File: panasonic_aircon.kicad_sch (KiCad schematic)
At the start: 24 parts, among them J1 Conn_01x04, Q1 BSS138, Q2 BSS138, SW1 SW_Push, U1 ESP32-WROOM-32, U2 AP2112K-3.3, U3 ESP_Programmer

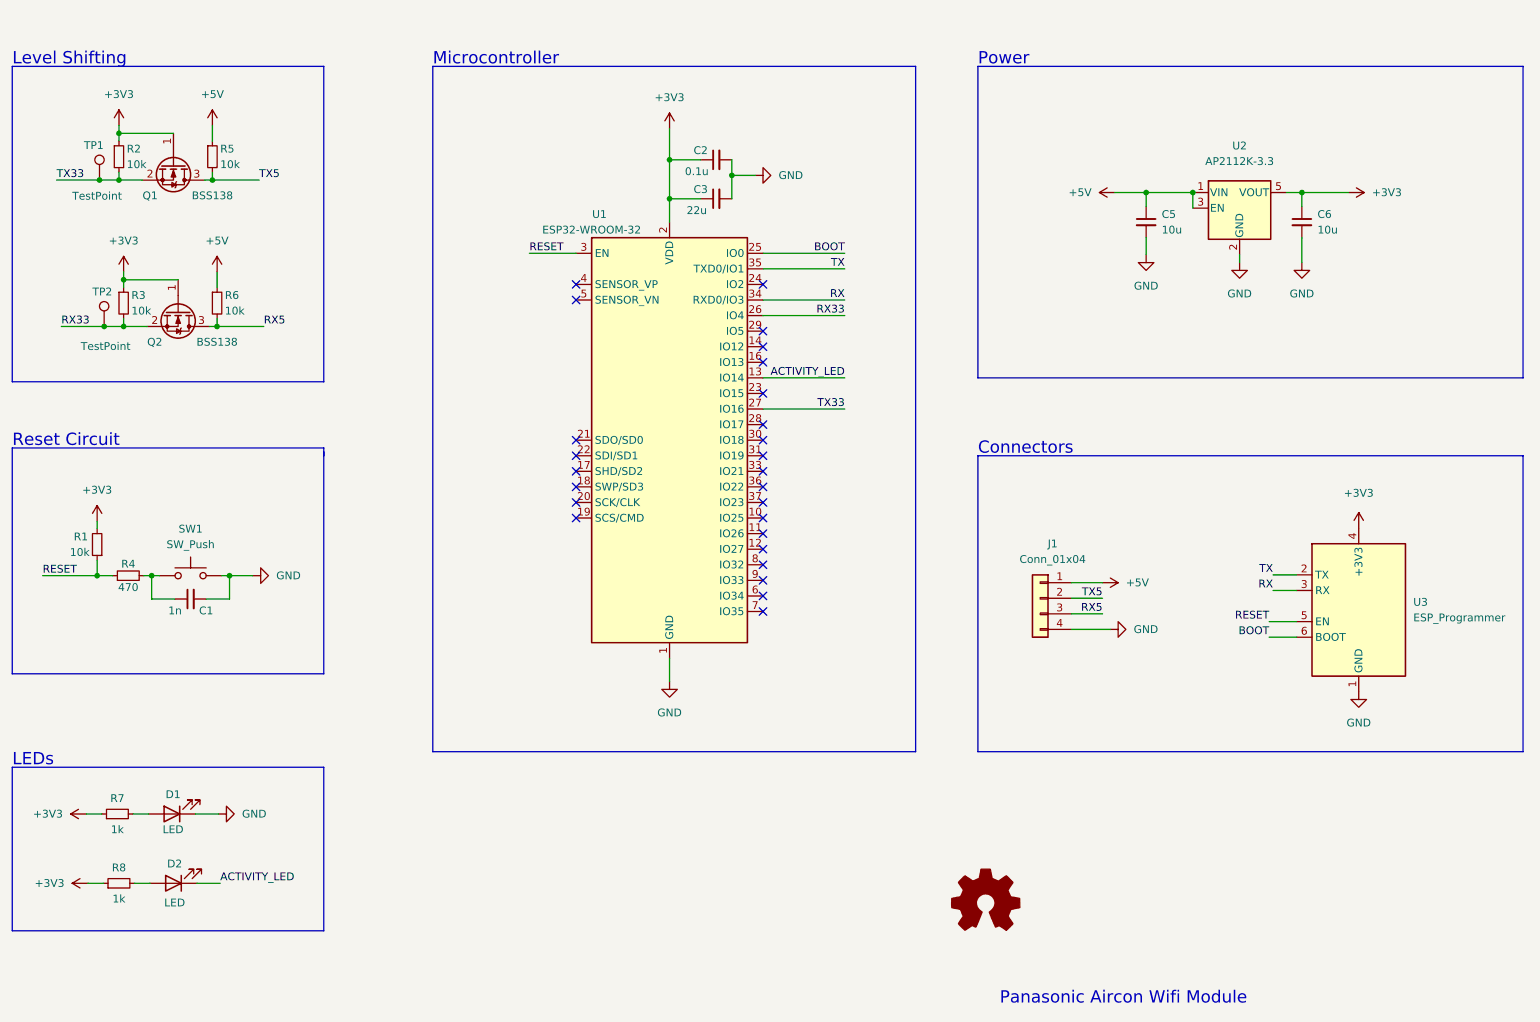
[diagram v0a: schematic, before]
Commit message: Using a simple BC807 for open collector TX signal. NXP level shifter design could force to 0 the MCU PP pin if some devices are transmitting on the TxD line. Panasonic permits to connect more remote controllers on the same bus.
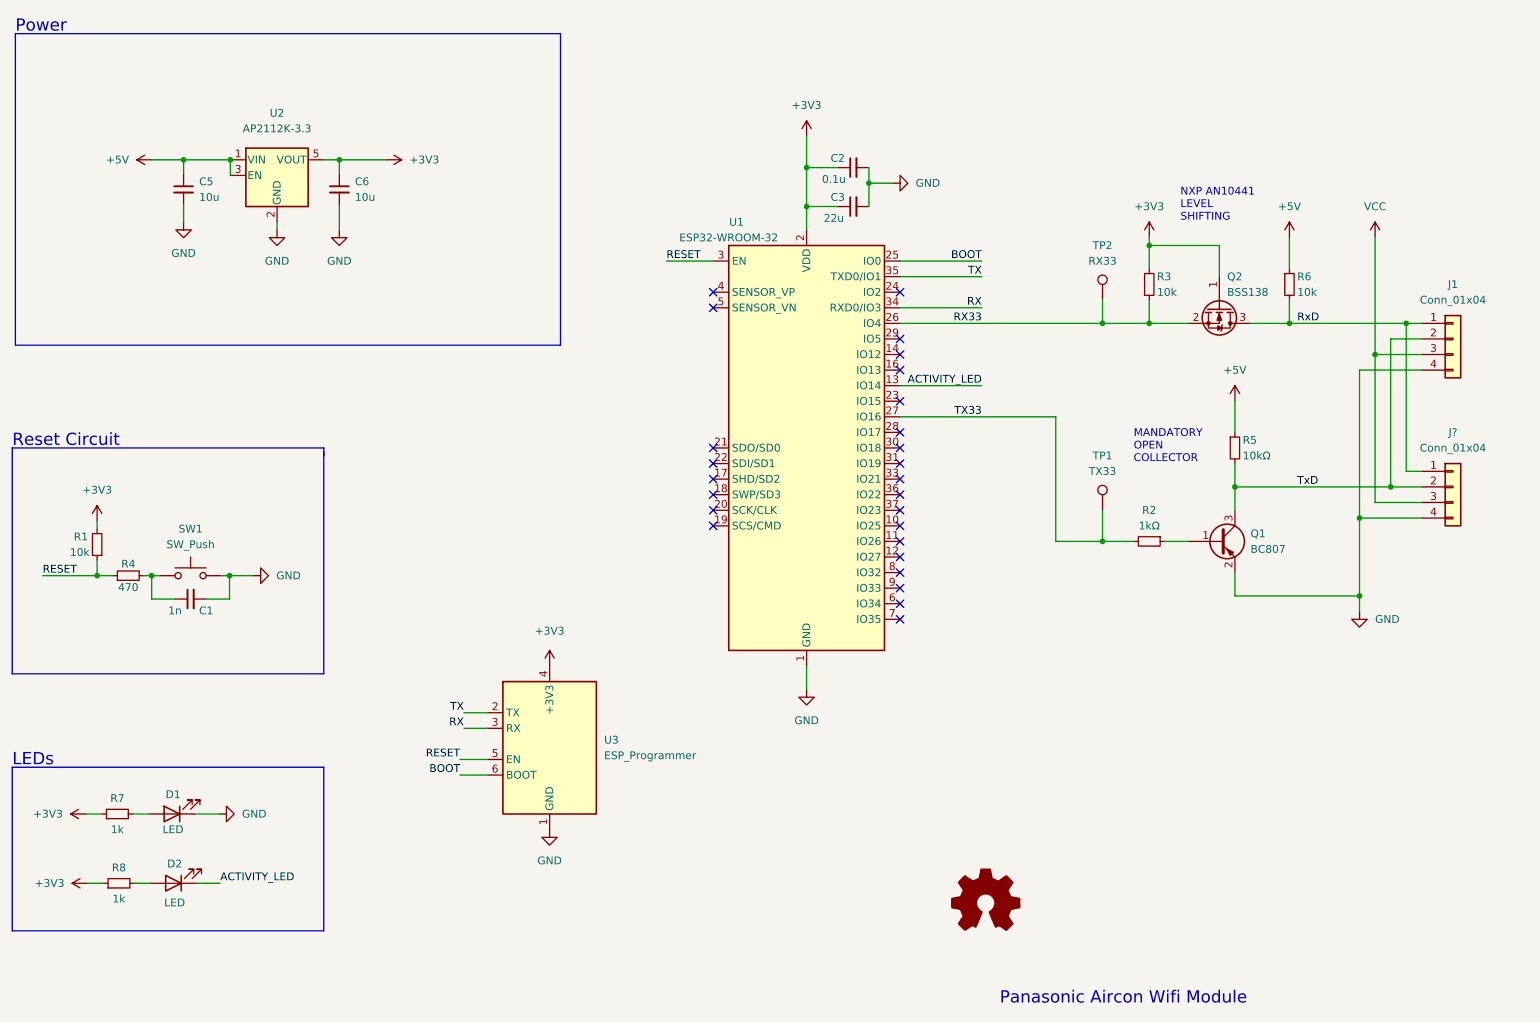
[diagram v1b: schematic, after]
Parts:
- removed Q1: BSS138, Package_TO_SOT_SMD:SOT-23, symbol Transistor_FET:BSS138
- added J?: Conn_01x04, Connector_Molex:Molex_PicoBlade_53048-0410_1x04_P1.25mm_Horizontal, symbol Connector_Generic:Conn_01x04
- added Q1: BC807, Package_TO_SOT_SMD:SOT-23, symbol Transistor_BJT:BC807
- R2: value 10k -> 1kΩ
- R5: value 10k -> 10kΩ
- TP1: value TestPoint -> TX33
- TP2: value TestPoint -> RX33
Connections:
- net +3V3: no longer R2.1
- net +5V: no longer J1.1 (Pin_1)
- net GND: now also J?.4 (Pin_4), Q1.2 (E)
- net RX5 renamed RxD
- net RxD: now also J1.1 (Pin_1), J?.1 (Pin_1); no longer J1.3 (Pin_3)
- net TX5 renamed TxD
- net TxD: now also J?.2 (Pin_2), Q1.3 (C)
- new net: Q1.1 (B), R2.1
- new net VCC: J1.3 (Pin_3), J?.3 (Pin_3)
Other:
- note added: "MANDATORY OPEN COLLECTOR"
- note added: "NXP AN10441 LEVEL SHIFTING"
- note removed: "Connectors"
- note removed: "Level Shifting"
- note removed: "Microcontroller"
- moved on the sheet: C5, C6, U2, U3

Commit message: Added a ferrite coil on bus power supply to prevent noises (value TBA)
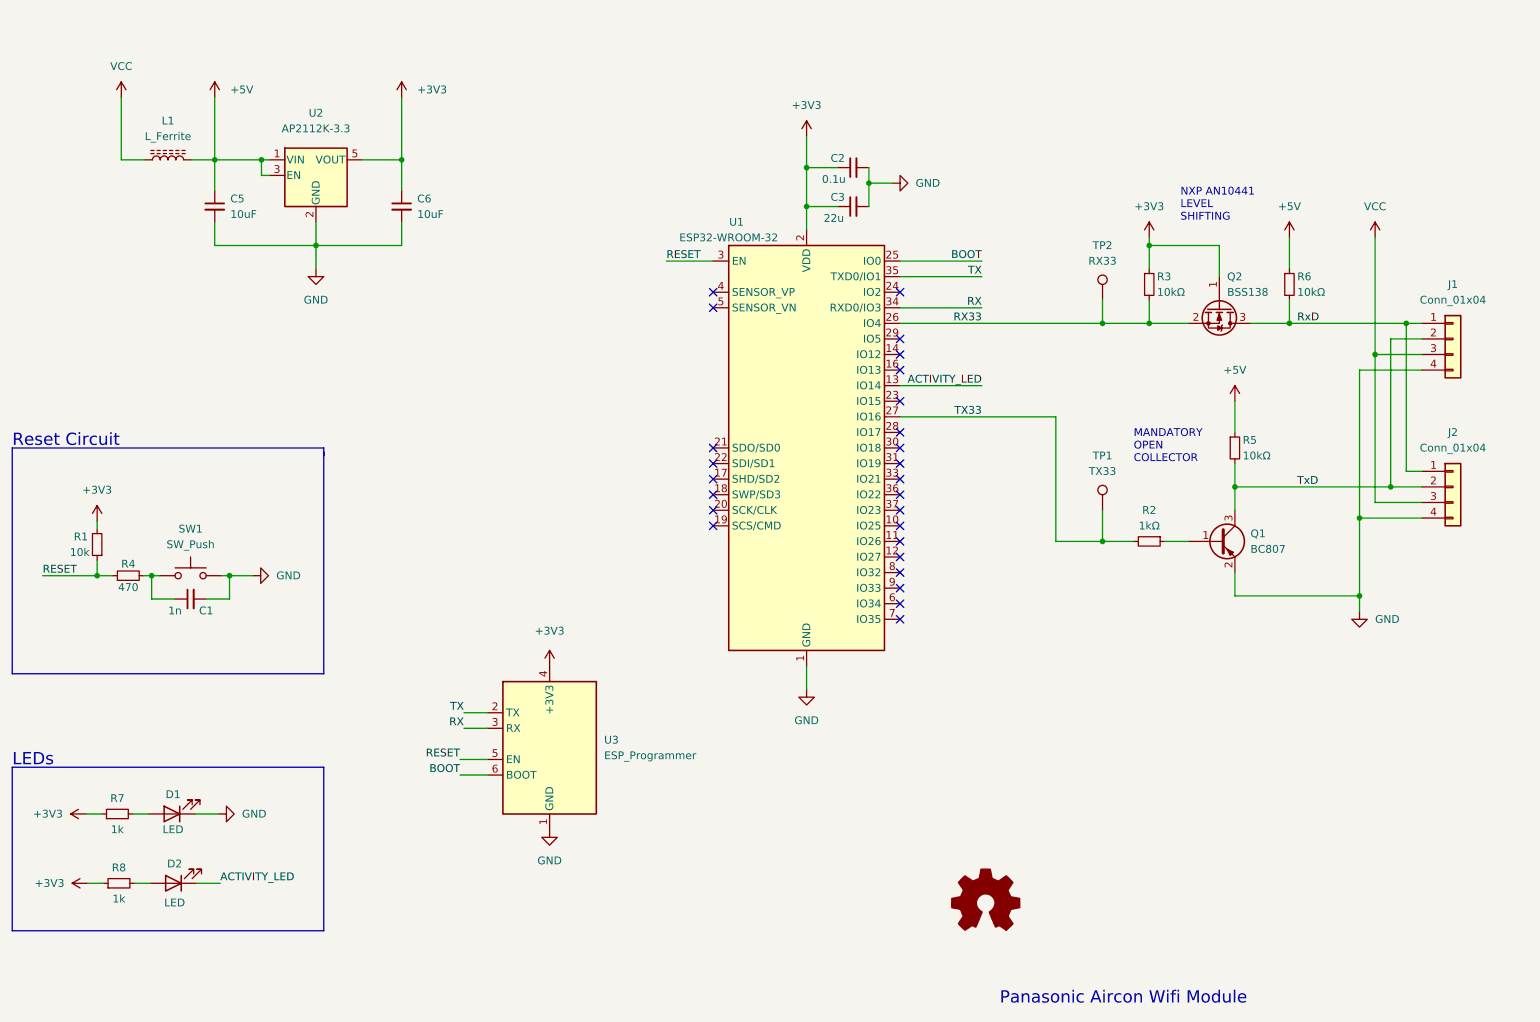
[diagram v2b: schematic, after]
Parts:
- added L1: L_Ferrite, symbol Device:L_Ferrite
- C5, C6: value 10u -> 10uF
- R3, R6: value 10k -> 10kΩ
- gave numbers to parts that had none: 1
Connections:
- net +5V: now also L1.2
- net VCC: now also L1.1
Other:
- note removed: "Power"
